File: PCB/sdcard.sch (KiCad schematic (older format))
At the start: 4 parts, among them J24 Micro_SD_Card_Det_Hirose_DM3AT

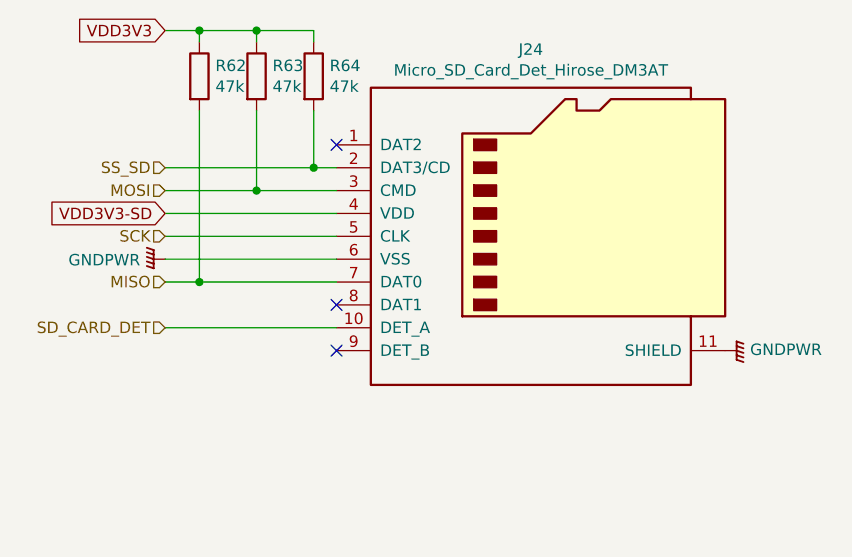
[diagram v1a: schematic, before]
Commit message: Fixes of v1.3 errors
 * Fixed missing GND connection for SD card detect
 * Optimized solder mask clearance from 0.2 to 0.05
 * Changed 3.3V LDO
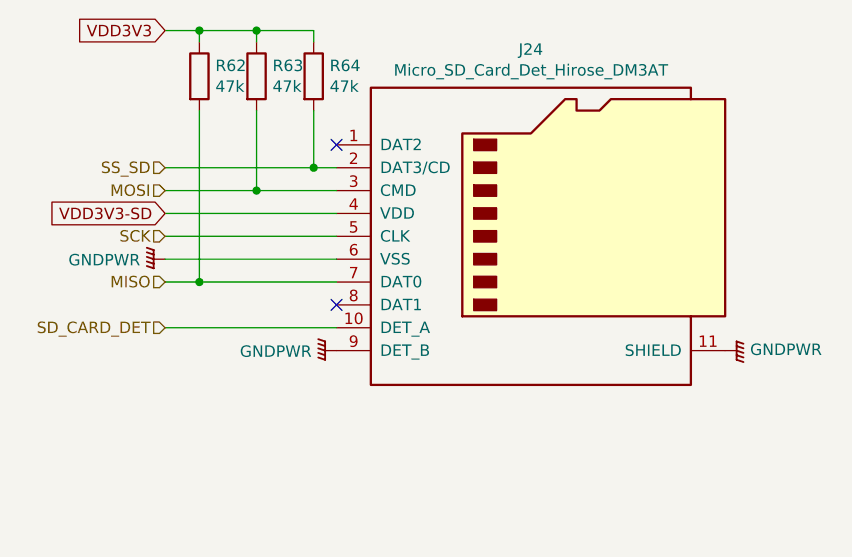
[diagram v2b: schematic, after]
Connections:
- net GNDPWR: now also J24.9 (DET_B)
- no-connect marks 3 -> 2
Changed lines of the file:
@@
 NoConn ~ 5150 3000
 NoConn ~ 5150 3700
-NoConn ~ 5150 3900
+$Comp
+L power:GNDPWR #PWR?
+U 1 1 5BE683A1
+P 5150 3900
+F 0 "#PWR?" H 5150 3700 50  0001 C CNN
+F 1 "GNDPWR" V 5154 3791 50  0000 R CNN
+F 2 "" H 5150 3850 50  0001 C CNN
+F 3 "" H 5150 3850 50  0001 C CNN
+	1    5150 3900
+	0    1    1    0
+$EndComp
 $EndSCHEMATC

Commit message: Fixed BOM and some footprint issues.
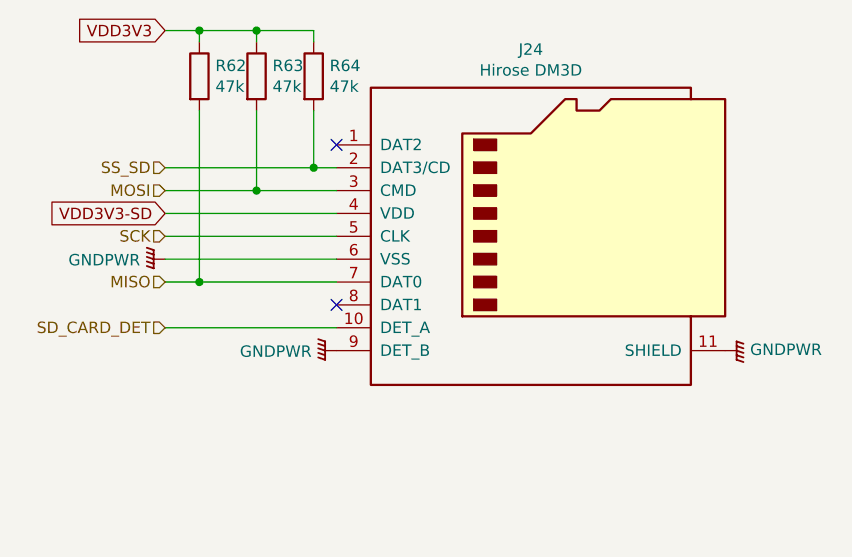
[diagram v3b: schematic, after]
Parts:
- J24: value Micro_SD_Card_Det_Hirose_DM3AT -> Hirose DM3D
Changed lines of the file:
@@
 P 6050 3400
 F 0 "J24" H 6000 4217 50  0000 C CNN
-F 1 "Micro_SD_Card_Det_Hirose_DM3AT" H 6000 4126 50  0000 C CNN
+F 1 "Hirose DM3D" H 6000 4126 50  0000 C CNN
 F 2 "custom-footprints:microSD_HC_Hirose_DM3D-SF" H 8100 4100 50  0001 C CNN
 F 3 "https://www.hirose.com/product/en/download_file/key_name/DM3/category/Catalog/doc_file_id/49662/?file_category_id=4&item_id=195&is_series=1" H 6050 3500 50  0001 C CNN

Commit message: Add PD for SPI SCK and some footprint fixes
Footprint fixes are mainly orientation markings.
PD needed for missbehaving Marlin firmware.
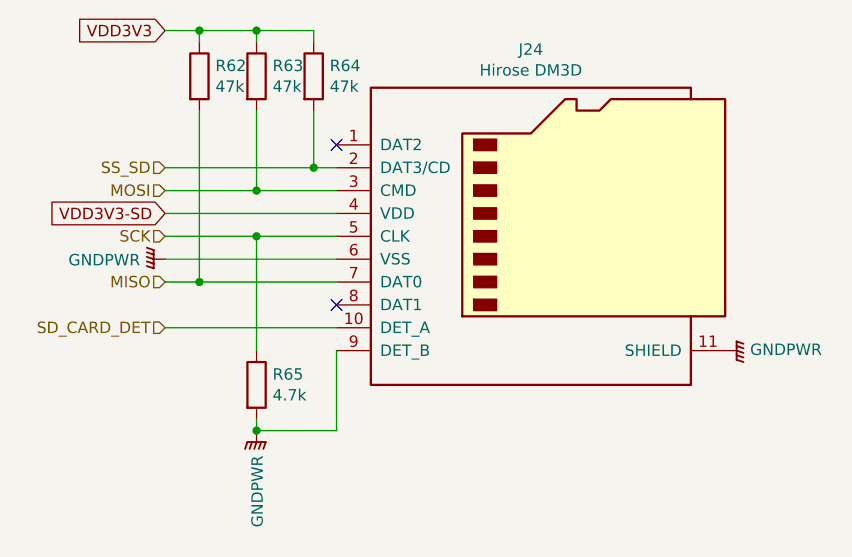
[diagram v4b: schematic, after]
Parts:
- added R65: 4.7k, Resistor_SMD:R_0603_1608Metric, symbol Device:R
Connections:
- net GNDPWR: now also R65.2
- net SCK: now also R65.1
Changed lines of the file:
@@
 	4400 3300 5150 3300
 Wire Wire Line
-	5150 3400 4400 3400
+	5150 3400 4800 3400
 Wire Wire Line
 	4400 3500 5150 3500
@@
 NoConn ~ 5150 3700
 $Comp
-L power:GNDPWR #PWR?
+L power:GNDPWR #PWR0150
 U 1 1 5BE683A1
-P 5150 3900
-F 0 "#PWR?" H 5150 3700 50  0001 C CNN
-F 1 "GNDPWR" V 5154 3791 50  0000 R CNN
-F 2 "" H 5150 3850 50  0001 C CNN
-F 3 "" H 5150 3850 50  0001 C CNN
-	1    5150 3900
-	0    1    1    0
+P 4800 4250
+F 0 "#PWR0150" H 4800 4050 50  0001 C CNN
+F 1 "GNDPWR" V 4804 4141 50  0000 R CNN
+F 2 "" H 4800 4200 50  0001 C CNN
+F 3 "" H 4800 4200 50  0001 C CNN
+	1    4800 4250
+	1    0    0    -1
 $EndComp
+$Comp
+L Device:R R65
+U 1 1 5C72C9C8
+P 4800 4050
+F 0 "R65" H 4870 4096 50  0000 L CNN
+F 1 "4.7k" H 4870 4005 50  0000 L CNN
+F 2 "Resistor_SMD:R_0603_1608Metric" V 4730 4050 50  0001 C CNN
+F 3 "~" H 4800 4050 50  0001 C CNN
+	1    4800 4050
+	1    0    0    -1
+$EndComp
+Wire Wire Line
+	4800 4250 5150 4250
+Wire Wire Line
+	5150 4250 5150 3900
+Wire Wire Line
+	4800 4200 4800 4250
+Connection ~ 4800 4250
+Wire Wire Line
+	4800 3900 4800 3400
+Connection ~ 4800 3400
+Wire Wire Line
+	4800 3400 4400 3400
 $EndSCHEMATC
